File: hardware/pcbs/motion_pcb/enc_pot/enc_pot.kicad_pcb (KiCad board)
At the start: 2 copper layers, 11 parts

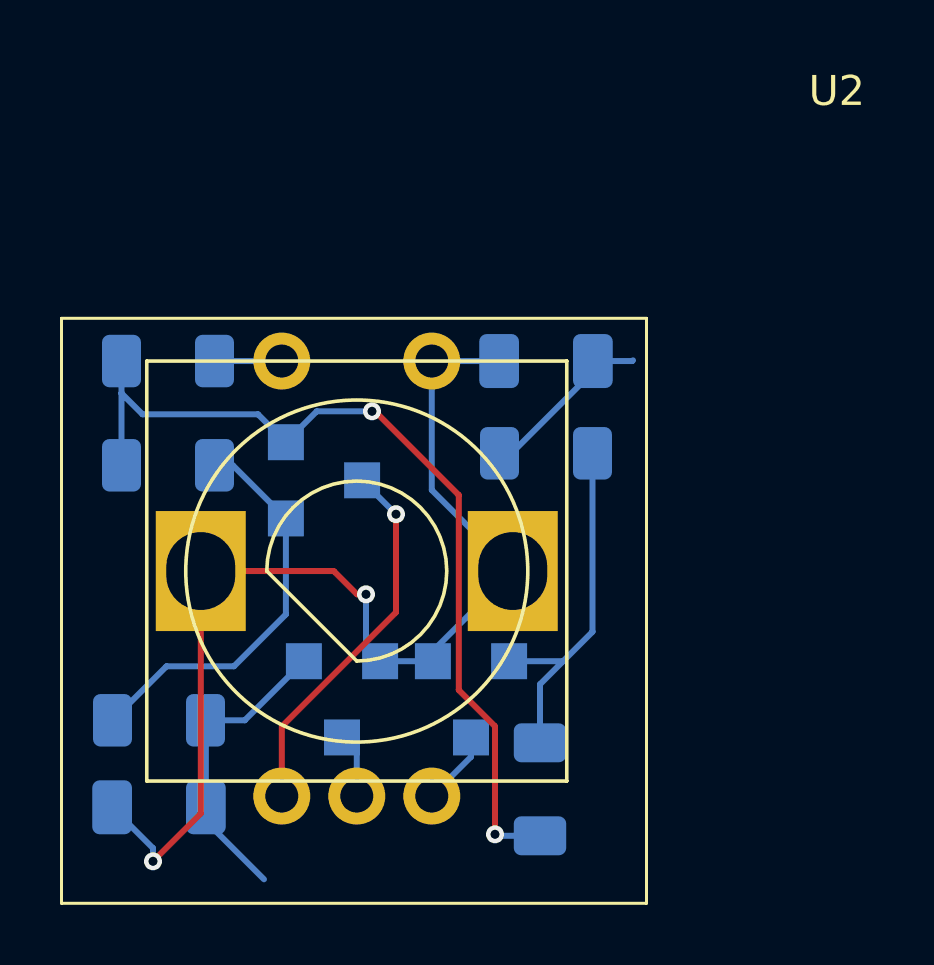
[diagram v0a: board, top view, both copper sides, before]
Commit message: changing labels
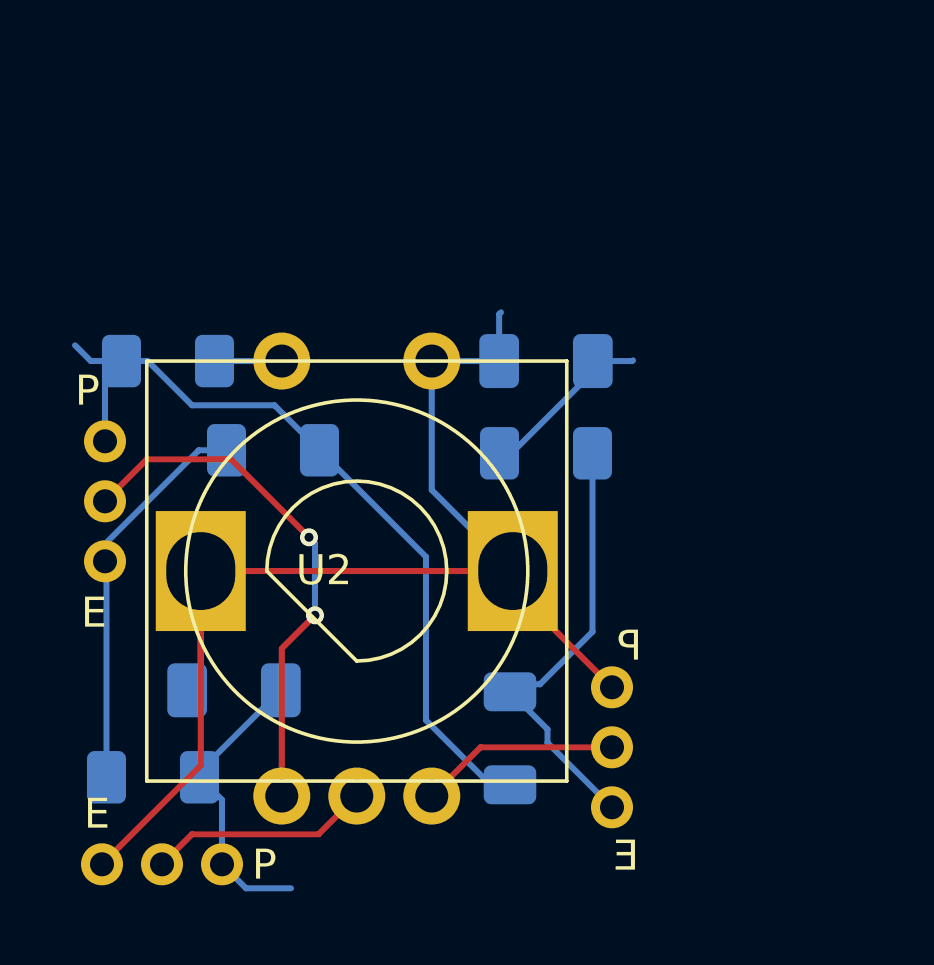
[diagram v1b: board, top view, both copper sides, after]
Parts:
- U1, U3, U4: footprint 3dAudioFoot:A3_1and2 -> 3dAudioFoot:a3_jumper_fix
- moved U3 8.14 mm to (59.9, 73.7), turned to 90 degrees
- moved U1 7.33 mm to (58.0, 61.6)
- moved U4 4.96 mm to (74.9, 69.8), turned to 180 degrees
- moved C1 4.63 mm to (62.3, 67.9)
- moved R2 3.54 mm to (63.6, 59.9), turned to 180 degrees
- moved R4 1.97 mm to (71.5, 69.5)
- moved R1 1.91 mm to (59.6, 70.8)
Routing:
- net GND: track 37.2 -> 43.0 mm, vias 2 -> 0
- net Net-(U2-EGND/PW): track 2.16 -> 7.43 mm
- net Net-(U2-E1/PA): track 12.6 -> 17.6 mm, vias 1 -> 2
- net Net-(U2-E2/PB): track 2.50 -> 6.68 mm
- net +3V3: track 30.5 -> 26.7 mm, vias 2 -> 0
- net Net-(R4-Pad2): track 12.2 -> 14.8 mm
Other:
- board text removed: "S"
